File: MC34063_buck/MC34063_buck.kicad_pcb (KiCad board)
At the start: 2 copper layers, 88.6 x 24 mm, 23 parts, among them J1 INPUT, J2 OUTPUT, Q1 2N2222, U1 MC34063AP

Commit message: Gerbers
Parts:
- C2: value 100p -> 22p
- L1: value 10u -> 100u

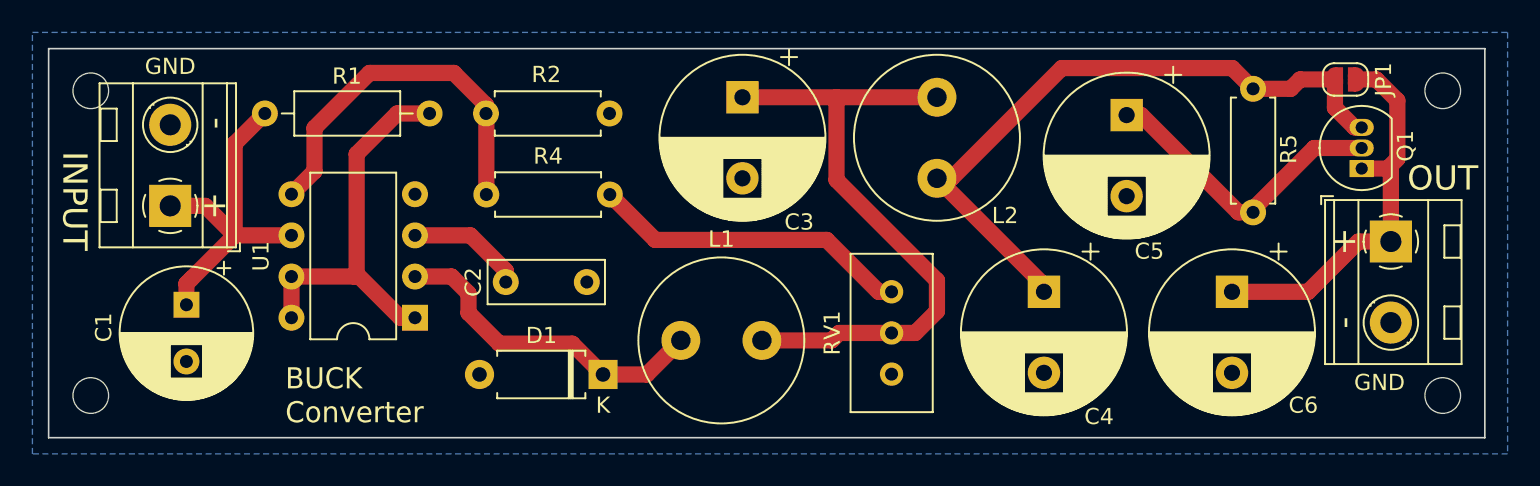
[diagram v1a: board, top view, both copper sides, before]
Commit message: Made buck & inverter PCB's smaller for panelization
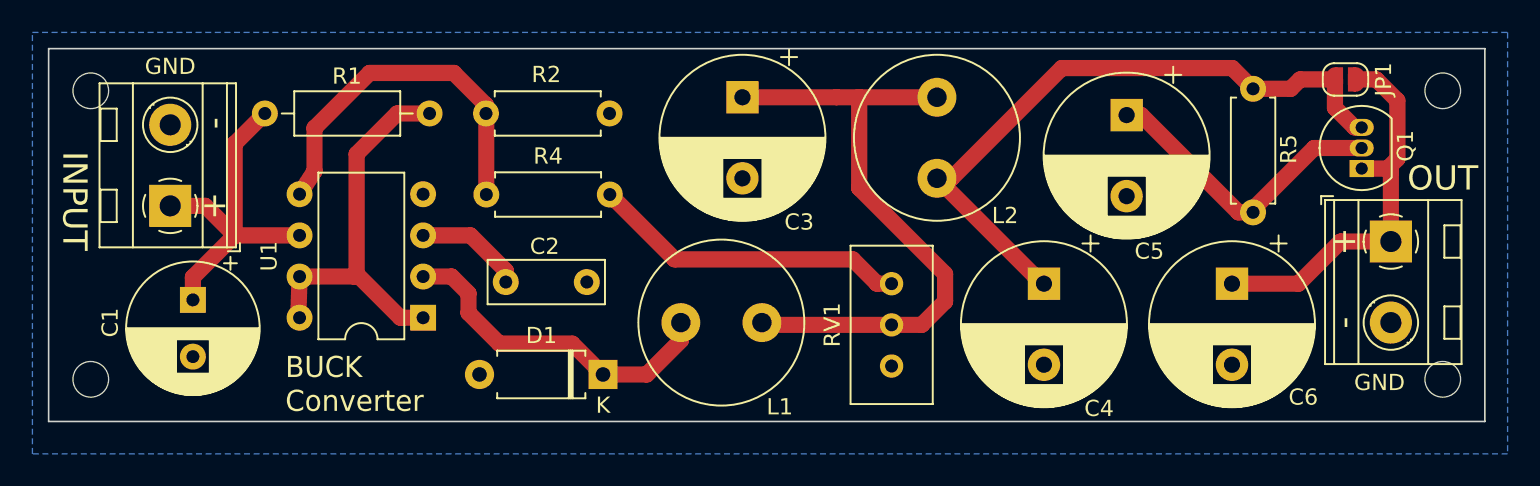
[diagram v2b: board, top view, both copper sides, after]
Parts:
- moved L1 1.10 mm to (84.0, 75.9)
- moved H1 1.00 mm to (47.6, 79.4)
- moved H4 1.00 mm to (131.0, 79.4)
- moved C4 0.50 mm to (106.4, 73.5)
- moved C6 0.50 mm to (118.0, 73.5)
- moved RV1 0.50 mm to (97.0, 73.5)
- moved U1 0.50 mm to (68.1, 75.6)
- moved C1 0.50 mm to (53.9, 74.5)
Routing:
- net Net-(D1-Pad1): track 20.5 -> 21.1 mm
- net Net-(C3-Pad1): track 39.3 -> 38.7 mm
- net Net-(C2-Pad1): track 7.20 -> 6.70 mm
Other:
- board size 88.6 x 24 mm -> 88.6 x 23 mm
